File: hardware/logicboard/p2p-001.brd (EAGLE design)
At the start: 72 x 72 mm, 28 parts, among them IC11 74ALS04N, J0 DC9V, J11 AUDIO_JACK_3.5MM_PTH, J12 AUDIO_JACK_3.5MM_PTH, J13 AUDIO_JACK_3.5MM_PTH, J14 AUDIO_JACK_3.5MM_PTH, J7 DIN5, J8 DIN5, J9 DIN5, X0 MKDSN1,5/2-5,08

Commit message: Silk.
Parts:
- turned L0/1 to 90 degrees
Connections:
- net MRXDTCT renamed NDX
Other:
- board text added: "0"
- board text added: "BackPort II"
- board text added: "GeekPort II"
- board text added: "Port Replicator 2.6.3-A"
- board text removed: "BackPort 2.0"
- board text removed: "GeekPort 2.0"
- board text removed: "Port Replicator 1.0.1-A"
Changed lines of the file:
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@@
 <text x="36" y="34" size="1.27" layer="25" align="bottom-center">Pineapple II</text>
 <wire x1="0" y1="69" x2="0" y2="3" width="0" layer="20"/>
-<text x="22" y="34.5" size="1" layer="25" align="center">Port Replicator 1.0.1-A</text>
+<text x="36" y="24" size="1" layer="25" align="center">Port Replicator 2.6.3-A</text>
 <wire x1="72" y1="3" x2="72" y2="69" width="0" layer="20"/>
 <wire x1="72" y1="69" x2="69" y2="72" width="0" layer="20" curve="90"/>
@@
 <text x="71" y="13" size="1" layer="26" rot="MR90" align="top-center">DC9-12V</text>
 <text x="66" y="15.54" size="1" layer="26" rot="MR90" align="center">+</text>
-<text x="4.5" y="60.73" size="1" layer="25" align="center">1</text>
-<text x="1.5" y="63.27" size="1" layer="25" align="center">2</text>
+<text x="4.5" y="60.75" size="1" layer="25" align="center">0</text>
+<text x="1.5" y="63.25" size="1" layer="25" align="center">1</text>
 <text x="6" y="56.27" size="1" layer="26" rot="MR90" align="center">K</text>
 <text x="6" y="62" size="1" layer="26" rot="MR90" align="center">K</text>
@@
 </polygon>
 <text x="31" y="29.5" size="1" layer="25" align="center">RST</text>
-<text x="16" y="28" size="1" layer="25" rot="R90" align="center">GeekPort 2.0</text>
-<text x="56" y="36" size="1" layer="25" rot="R90" align="center">BackPort 2.0</text>
+<text x="16" y="28" size="1" layer="25" rot="R90" align="center">GeekPort II</text>
+<text x="56" y="36" size="1" layer="25" rot="R90" align="center">BackPort II</text>
 </plain>
 <attributes>
@@
 <attribute name="VALUE" x="6.175" y="6.19" size="1.27" layer="27" rot="R90"/>
 </element>
-<element name="L0/1" library="led" library_urn="urn:adsk.eagle:library:259" package="DUOLED-C-5MM" package3d_urn="urn:adsk.eagle:package:15851/1" value="" x="3" y="62" smashed="yes" rot="R270">
-<attribute name="NAME" x="3" y="66" size="1" layer="25" ratio="10" align="center"/>
-<attribute name="POPULARITY" value="1" x="3" y="62" size="1.778" layer="27" rot="R270" display="off"/>
-<attribute name="VALUE" x="0.46" y="58.19" size="1.27" layer="27" ratio="10" rot="R270"/>
+<element name="L0/1" library="led" library_urn="urn:adsk.eagle:library:259" package="DUOLED-C-5MM" package3d_urn="urn:adsk.eagle:package:15851/1" value="" x="3" y="62" smashed="yes" rot="R90">
+<attribute name="NAME" x="3" y="66" size="1" layer="25" ratio="10" rot="R180" align="center"/>
+<attribute name="POPULARITY" value="1" x="3" y="62" size="1.778" layer="27" rot="R90" display="off"/>
+<attribute name="VALUE" x="5.54" y="65.81" size="1.27" layer="27" ratio="10" rot="R90"/>
 </element>
 <element name="RN1" library="resistor-net" library_urn="urn:adsk.eagle:library:343" package="RN-5" package3d_urn="urn:adsk.eagle:package:24976/1" value="" x="22" y="22" smashed="yes" rot="R270">
@@
 <wire x1="36" y1="41.69" x2="20.46" y2="48" width="0" layer="19" extent="1-1"/>
 </signal>
-<signal name="MRXDTCT">
+<signal name="NDX">
 <contactref element="SV2" pad="4"/>
 </signal>
@@
 <contactref element="L0/1" pad="AR"/>
 <contactref element="R10" pad="1"/>
-<wire x1="20.46" y1="43" x2="3" y2="59.46" width="0" layer="19" extent="1-1"/>
+<wire x1="20.46" y1="43" x2="3" y2="64.54" width="0" layer="19" extent="1-1"/>
 </signal>
 <signal name="LED0A">
 <contactref element="L0/1" pad="AX"/>
 <contactref element="R11" pad="2"/>
-<wire x1="25.54" y1="40.5" x2="3" y2="64.54" width="0" layer="19" extent="1-1"/>
+<wire x1="3" y1="59.46" x2="25.54" y2="40.5" width="0" layer="19" extent="1-1"/>
 </signal>
 </signals>

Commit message: Cloud work...
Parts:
- removed R10, R11, R2, R3: (no value), rcl:0204/5
- added L11, L12, L13, L14: OUT, led:LED3MM
- RN2: device resistor-net:RN-5 -> resistor-net:RN-9
- moved RN1 14.1 mm to (20.0, 36.0)
- moved RN2 14.1 mm to (52.0, 36.0)
- moved R00 1.12 mm to (24.0, 46.0), turned to 270 degrees
- moved C11 1.00 mm to (48.0, 46.0)
- moved IC11 0.50 mm to (36.0, 46.0)
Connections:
- removed net LED0A: L0/1.AX, R11.2
- removed net LED1A: L0/1.AR, R10.1
- removed net LEDMI: L2.K, R2.2
- removed net LEDMO: L3.K, R3.2
- new net N$10: IC11.6, L11.K
- new net N$12: L12.A, RN2.6
- new net N$13: L11.A, RN2.7
- new net N$3: L2.A, RN2.2
- new net N$4: L3.A, RN2.3
- new net N$5: L14.A, RN2.4
- new net N$6: L13.A, RN2.5
- new net N$7: IC11.12, L14.K
- new net N$8: IC11.10, L13.K
- new net N$9: IC11.8, L12.K
- net DTCT0: now also IC11.5
- net DTCT1: now also IC11.9
- net DTCT2: now also IC11.11
- net DTCT3: now also IC11.13
- net LED0: now also L0/1.AX; no longer R11.1
- net LED1: now also L0/1.AR; no longer R10.2
- net N$1: now also L2.K; no longer R2.1
- net N$2: now also L3.K; no longer R3.1
- net VCC: now also RN2.1; no longer L2.A, L3.A
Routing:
- net GND: track 0.00 -> 277.0 mm
- net LED1: track 0.00 -> 125.1 mm
- net LED0: track 0.00 -> 121.8 mm
- net VCC/2: track 0.00 -> 105.4 mm
- net V+: track 0.00 -> 104.9 mm, vias 0 -> 1
- net DTCT2: track 0.00 -> 97.0 mm, vias 0 -> 1
- net MISND: track 0.00 -> 92.7 mm
- net DTCT3: track 0.00 -> 90.9 mm
- net DTCT1: track 0.00 -> 89.3 mm
- net VCC: track 0.00 -> 70.6 mm, vias 0 -> 1
- net MTSND: track 0.00 -> 70.2 mm
- net MOSND: track 0.00 -> 64.0 mm, vias 0 -> 1
- net MIRTN: track 0.00 -> 59.1 mm
- net DTCT0: track 0.00 -> 58.4 mm
- net N$1: track 0.00 -> 57.2 mm
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
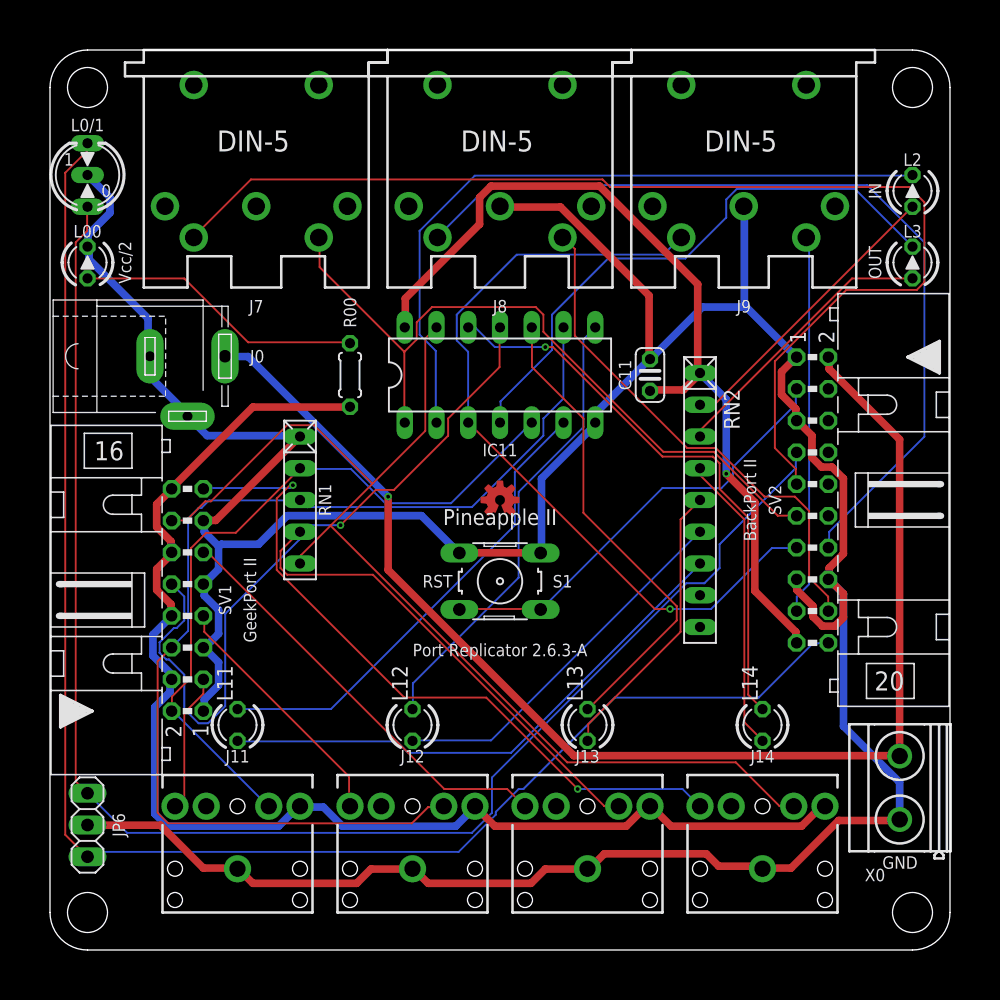
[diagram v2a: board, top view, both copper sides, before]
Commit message: GND pattern.
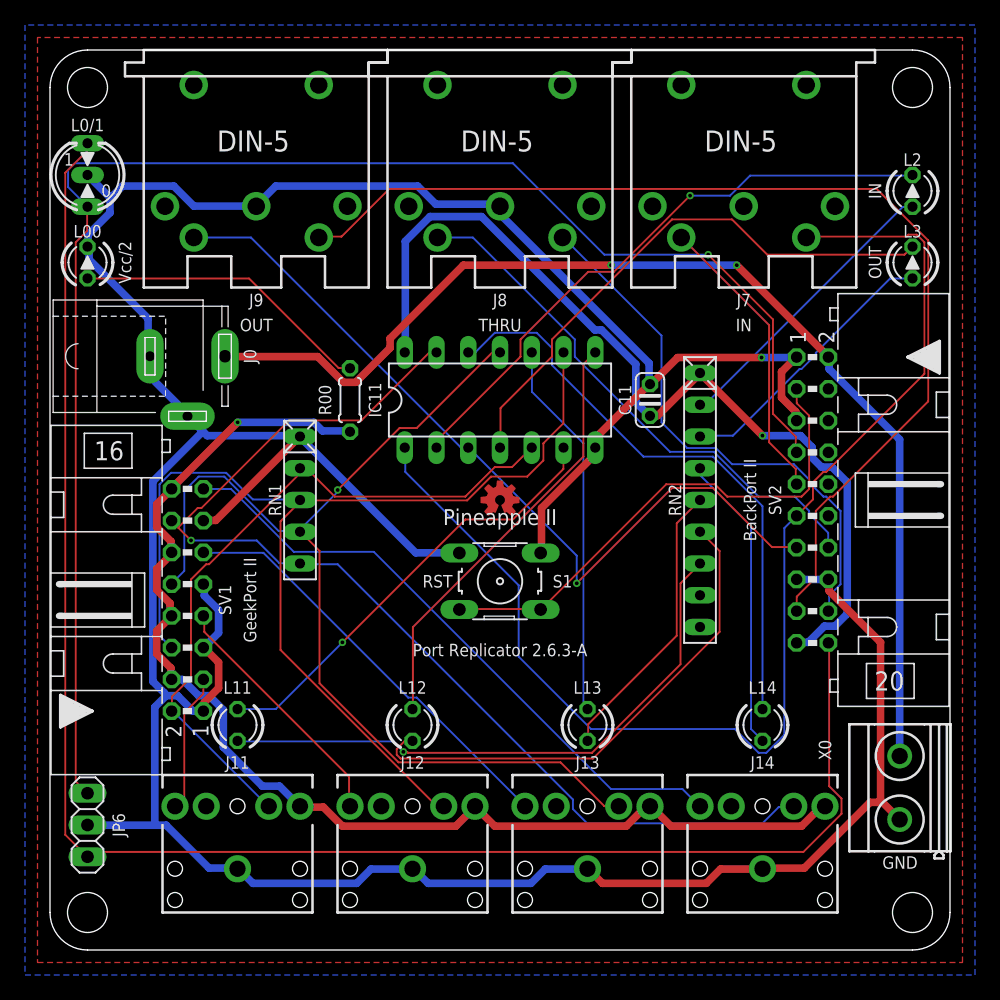
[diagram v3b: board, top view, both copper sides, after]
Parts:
- moved J7 39.0 mm to (55.5, 72.0)
- moved J9 39.0 mm to (16.5, 72.0)
- moved C11 2.00 mm to (48.0, 44.0)
- moved IC11 2.00 mm to (36.0, 44.0)
- moved R00 2.00 mm to (24.0, 44.0)
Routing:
- net MISND: track 92.7 -> 23.6 mm
- net MORTN: track 30.4 -> 86.2 mm
- net MIRTN: track 59.1 -> 99.6 mm
- net MTSND: track 70.2 -> 43.2 mm
- net GND: track 277.0 -> 293.3 mm, vias 0 -> 1
- net DTCT2: track 97.0 -> 82.4 mm
- net V+: track 104.9 -> 90.8 mm, vias 1 -> 2
- net N$12: track 29.9 -> 40.8 mm
- net LED1: track 125.1 -> 134.4 mm
- net N$1: track 57.2 -> 48.2 mm, vias 0 -> 1
- net VCC/2: track 105.4 -> 97.2 mm, vias 0 -> 1
- net N$8: track 38.3 -> 30.4 mm
- net ANLG3R: track 56.4 -> 50.2 mm, vias 2 -> 0
- net RST: track 35.5 -> 41.3 mm
- net VCC: track 70.6 -> 74.6 mm
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- added copper zone on layer 1, net GND
- added copper zone on layer 16, net GND
